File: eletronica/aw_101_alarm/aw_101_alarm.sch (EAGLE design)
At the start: 38 parts, among them IC1 ATTINY2313V, IC2 4511N, T2 2N2222, T3 2N2222, T4 2N2222, T5 2N2222, T6 2N2222, X1 UPDOWN, X2 TIMER, X3 STOPBTN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

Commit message: 
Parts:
- removed SG1: F/CM12P, buzzer:F/CM12P
- added X4: BUZZER, con-ptr500:AK500/2
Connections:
- net GND: now also X4-1.KL; no longer SG1.2
- net N$10: now also X4-2.KL; no longer SG1.1
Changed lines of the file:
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@@
 <part name="D1" library="diode" deviceset="1N4004" device=""/>
 <part name="D2" library="diode" deviceset="1N4004" device=""/>
-<part name="SG1" library="buzzer" deviceset="F/CM12P" device=""/>
 <part name="GND7" library="supply1" deviceset="GND" device=""/>
+<part name="X4" library="con-ptr500" deviceset="AK500/2" device="" value="BUZZER"/>
 </parts>
 <sheets>
@@
 <instance part="D1" gate="1" x="7.62" y="60.96"/>
 <instance part="D2" gate="1" x="15.24" y="66.04" rot="R270"/>
-<instance part="SG1" gate="G$1" x="88.9" y="27.94" rot="R270"/>
-<instance part="GND7" gate="1" x="86.36" y="20.32"/>
+<instance part="GND7" gate="1" x="86.36" y="25.4"/>
+<instance part="X4" gate="-1" x="91.44" y="27.94" rot="R180"/>
+<instance part="X4" gate="-2" x="91.44" y="30.48" rot="R180"/>
 </instances>
 <busses>
@@
 </segment>
 <segment>
-<pinref part="SG1" gate="G$1" pin="2"/>
+<pinref part="X4" gate="-1" pin="KL"/>
 <pinref part="GND7" gate="1" pin="GND"/>
 </segment>
@@
 <segment>
 <pinref part="IC1" gate="G$1" pin="(RXD)PD0"/>
-<pinref part="SG1" gate="G$1" pin="1"/>
 <wire x1="86.36" y1="40.64" x2="86.36" y2="30.48" width="0.1524" layer="91"/>
-</segment>
-</net>
+<pinref part="X4" gate="-2" pin="KL"/>
+</segment>
+</net>

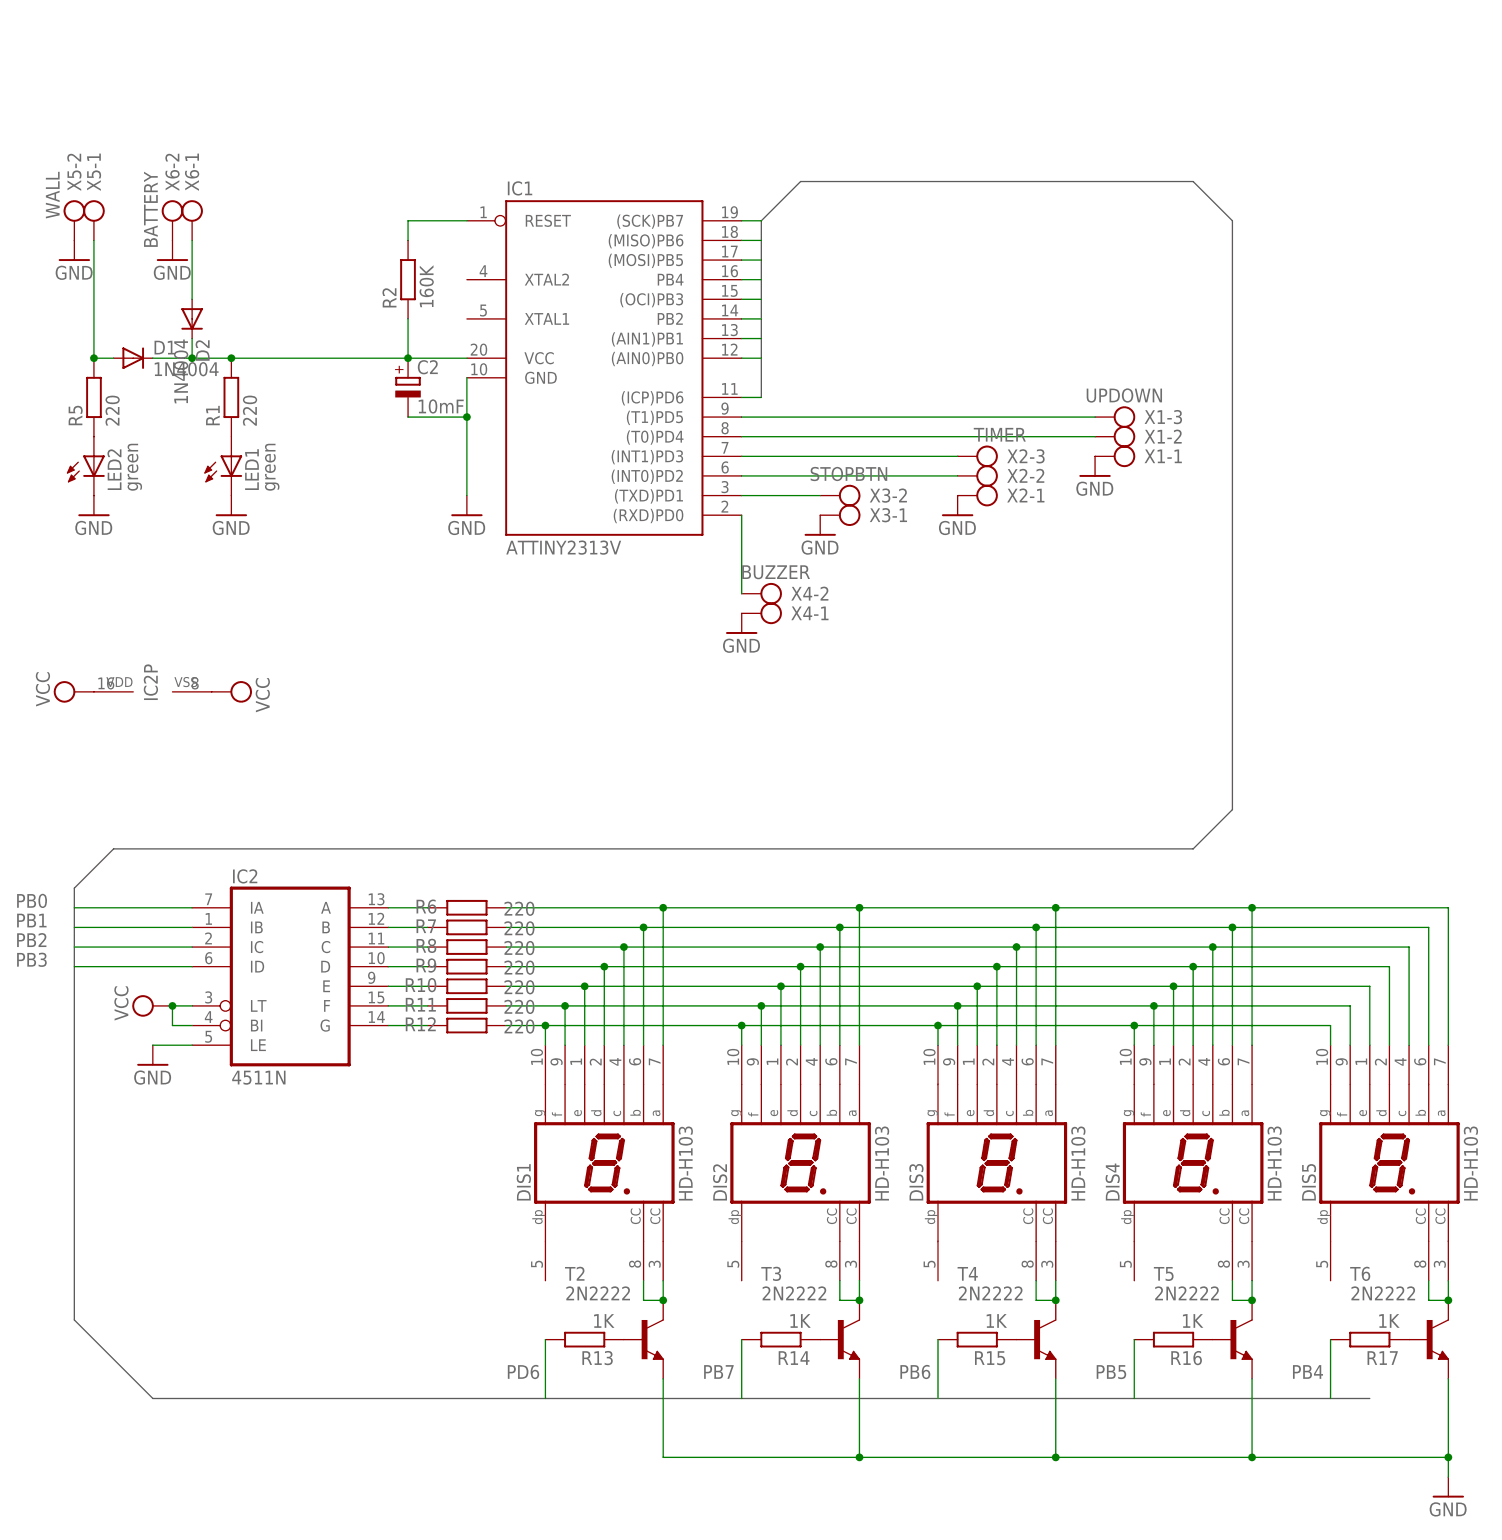
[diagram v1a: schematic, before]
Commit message: 
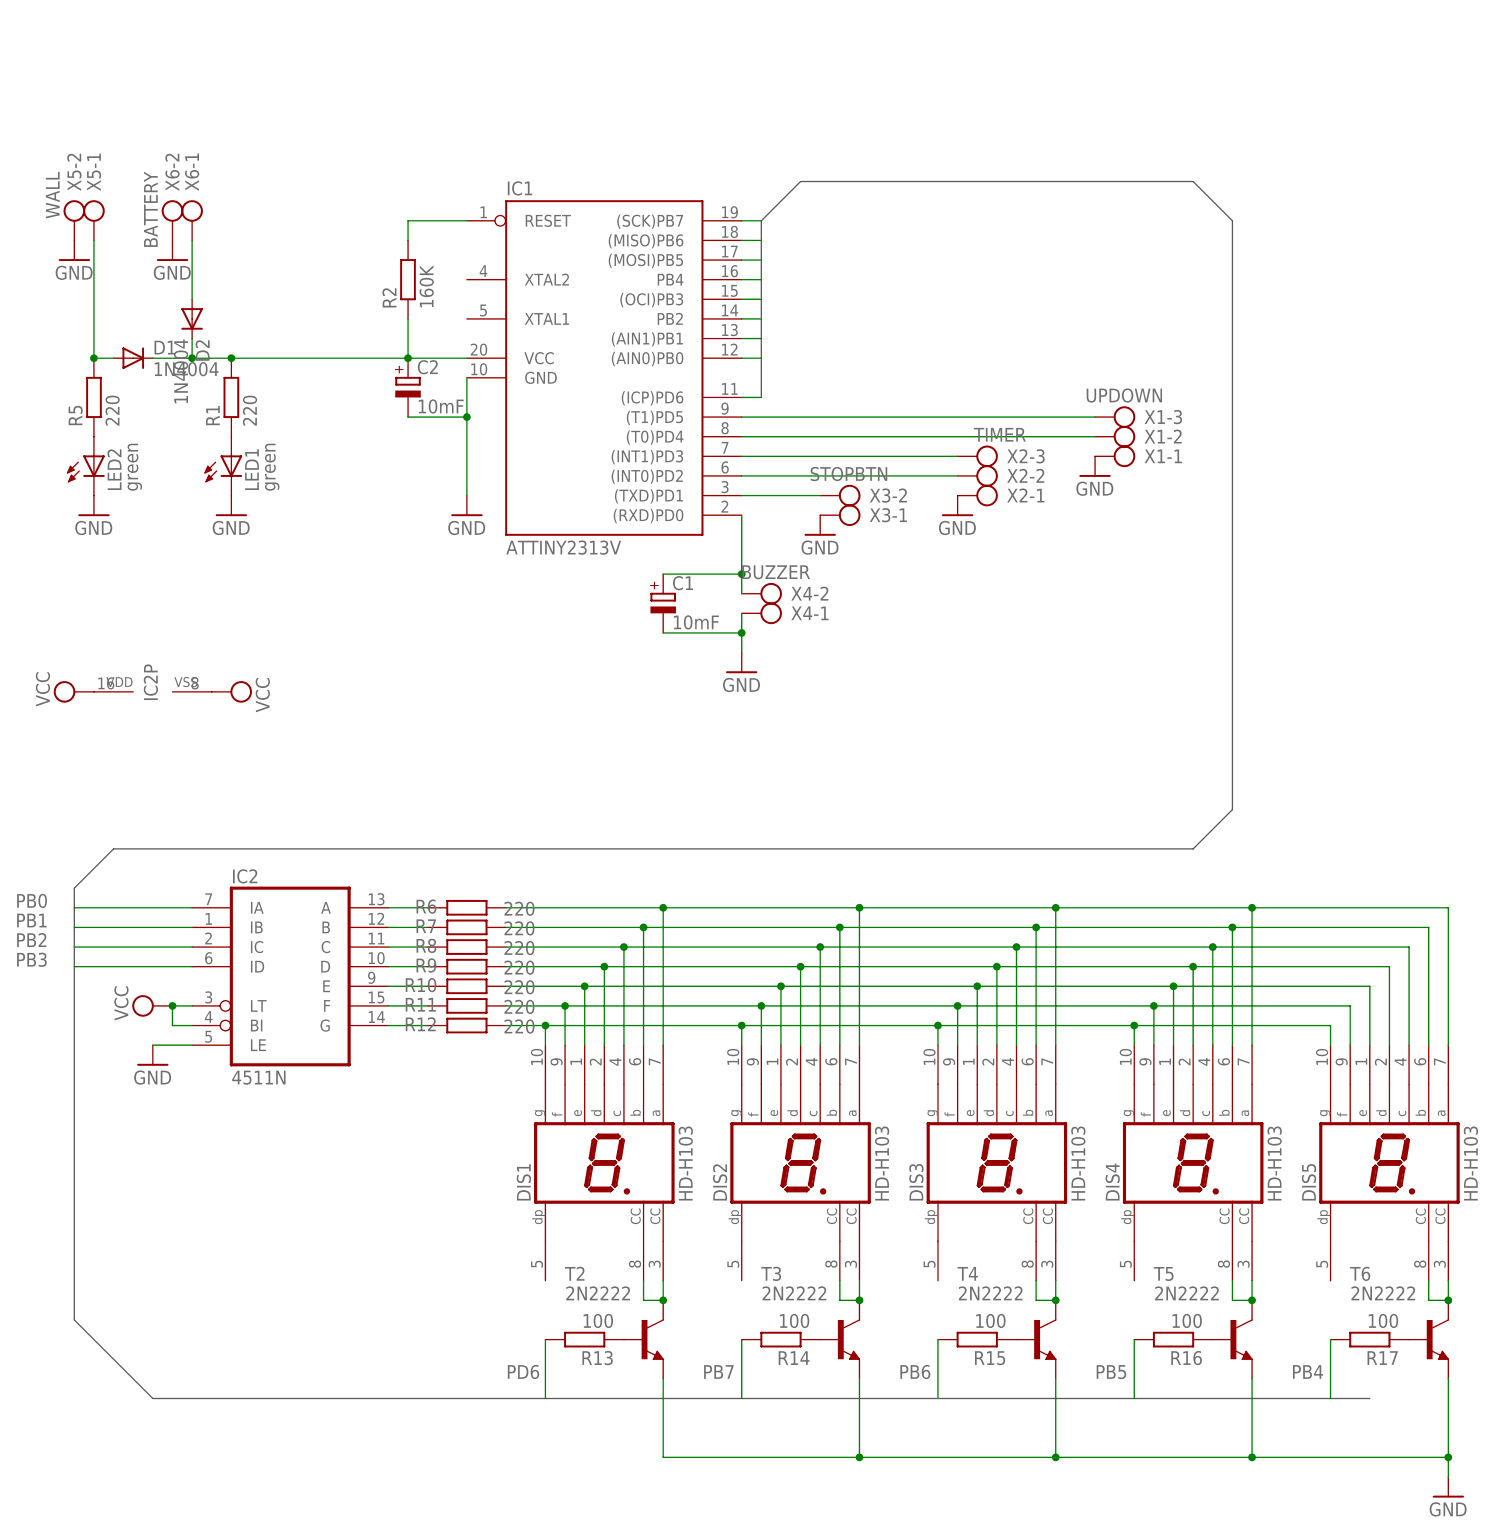
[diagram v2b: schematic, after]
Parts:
- added C1: 10mF, rcl:CPOL-EUE2.5-6
- R13, R14, R15, R16, R17: value 1K -> 100
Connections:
- net GND: now also C1.-
- net N$10: now also C1.+
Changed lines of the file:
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@@
 <part name="DIS5" library="display-hp" deviceset="HD-H103" device=""/>
 <part name="T2" library="transistor" deviceset="2N2222" device=""/>
-<part name="R13" library="rcl" deviceset="R-EU_" device="0207/10" value="1K"/>
+<part name="R13" library="rcl" deviceset="R-EU_" device="0207/10" value="100"/>
 <part name="T3" library="transistor" deviceset="2N2222" device=""/>
-<part name="R14" library="rcl" deviceset="R-EU_" device="0207/10" value="1K"/>
+<part name="R14" library="rcl" deviceset="R-EU_" device="0207/10" value="100"/>
 <part name="T4" library="transistor" deviceset="2N2222" device=""/>
-<part name="R15" library="rcl" deviceset="R-EU_" device="0207/10" value="1K"/>
+<part name="R15" library="rcl" deviceset="R-EU_" device="0207/10" value="100"/>
 <part name="T5" library="transistor" deviceset="2N2222" device=""/>
-<part name="R16" library="rcl" deviceset="R-EU_" device="0207/10" value="1K"/>
+<part name="R16" library="rcl" deviceset="R-EU_" device="0207/10" value="100"/>
 <part name="T6" library="transistor" deviceset="2N2222" device=""/>
-<part name="R17" library="rcl" deviceset="R-EU_" device="0207/10" value="1K"/>
+<part name="R17" library="rcl" deviceset="R-EU_" device="0207/10" value="100"/>
 <part name="GND9" library="supply1" deviceset="GND" device=""/>
 <part name="SUPPLY3" library="supply2" deviceset="VCC" device=""/>
@@
 <part name="GND7" library="supply1" deviceset="GND" device=""/>
 <part name="X4" library="con-ptr500" deviceset="AK500/2" device="" value="BUZZER"/>
+<part name="C1" library="rcl" deviceset="CPOL-EU" device="E2.5-6" value="10mF"/>
 </parts>
 <sheets>
@@
 <instance part="D1" gate="1" x="7.62" y="60.96"/>
 <instance part="D2" gate="1" x="15.24" y="66.04" rot="R270"/>
-<instance part="GND7" gate="1" x="86.36" y="25.4"/>
+<instance part="GND7" gate="1" x="86.36" y="20.32"/>
 <instance part="X4" gate="-1" x="91.44" y="27.94" rot="R180"/>
 <instance part="X4" gate="-2" x="91.44" y="30.48" rot="R180"/>
+<instance part="C1" gate="G$1" x="76.2" y="30.48"/>
 </instances>
 <busses>
@@
 <pinref part="X4" gate="-1" pin="KL"/>
 <pinref part="GND7" gate="1" pin="GND"/>
+<wire x1="86.36" y1="22.86" x2="86.36" y2="25.4" width="0.1524" layer="91"/>
+<pinref part="C1" gate="G$1" pin="-"/>
+<wire x1="86.36" y1="25.4" x2="86.36" y2="27.94" width="0.1524" layer="91"/>
+<wire x1="76.2" y1="25.4" x2="86.36" y2="25.4" width="0.1524" layer="91"/>
+<junction x="86.36" y="25.4"/>
 </segment>
 </net>
@@
 <segment>
 <pinref part="IC1" gate="G$1" pin="(RXD)PD0"/>
-<wire x1="86.36" y1="40.64" x2="86.36" y2="30.48" width="0.1524" layer="91"/>
+<wire x1="86.36" y1="40.64" x2="86.36" y2="33.02" width="0.1524" layer="91"/>
 <pinref part="X4" gate="-2" pin="KL"/>
-</segment>
-</net>
+<pinref part="C1" gate="G$1" pin="+"/>
+<wire x1="86.36" y1="33.02" x2="86.36" y2="30.48" width="0.1524" layer="91"/>
+<wire x1="76.2" y1="33.02" x2="86.36" y2="33.02" width="0.1524" layer="91"/>
+<junction x="86.36" y="33.02"/>
+</segment>
+</net>
